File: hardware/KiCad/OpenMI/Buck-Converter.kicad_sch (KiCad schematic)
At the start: 15 parts, among them U6 LM5163

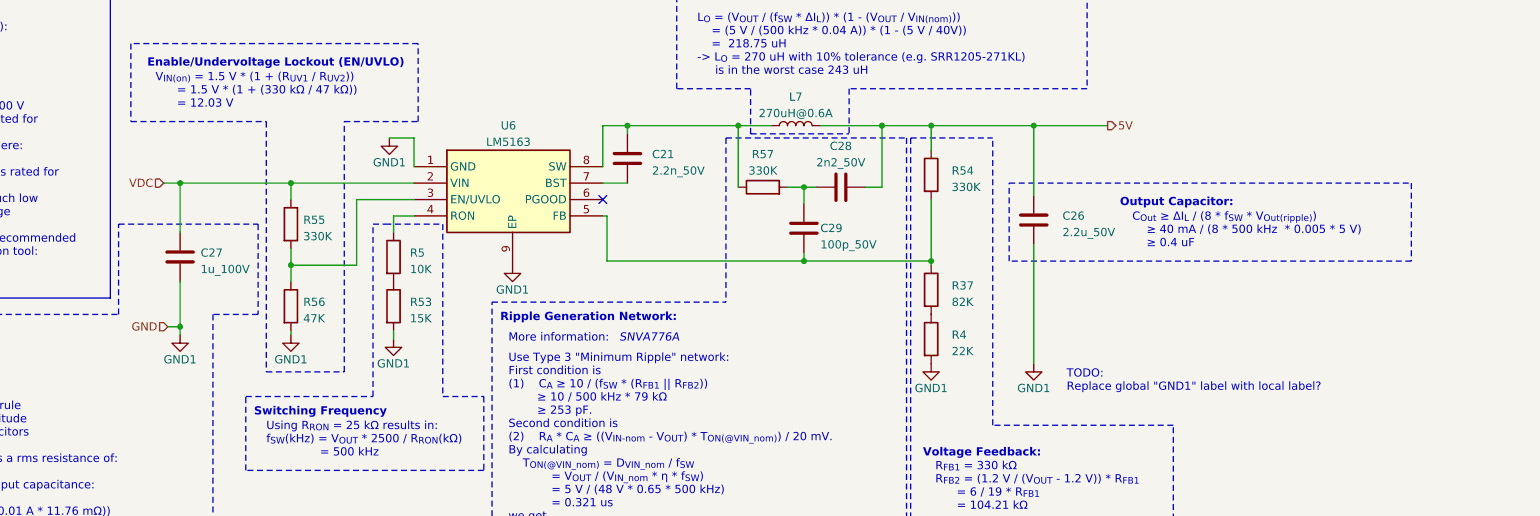
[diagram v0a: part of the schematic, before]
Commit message: refactor(hw): uses new symbol for `LM5163` buck converter
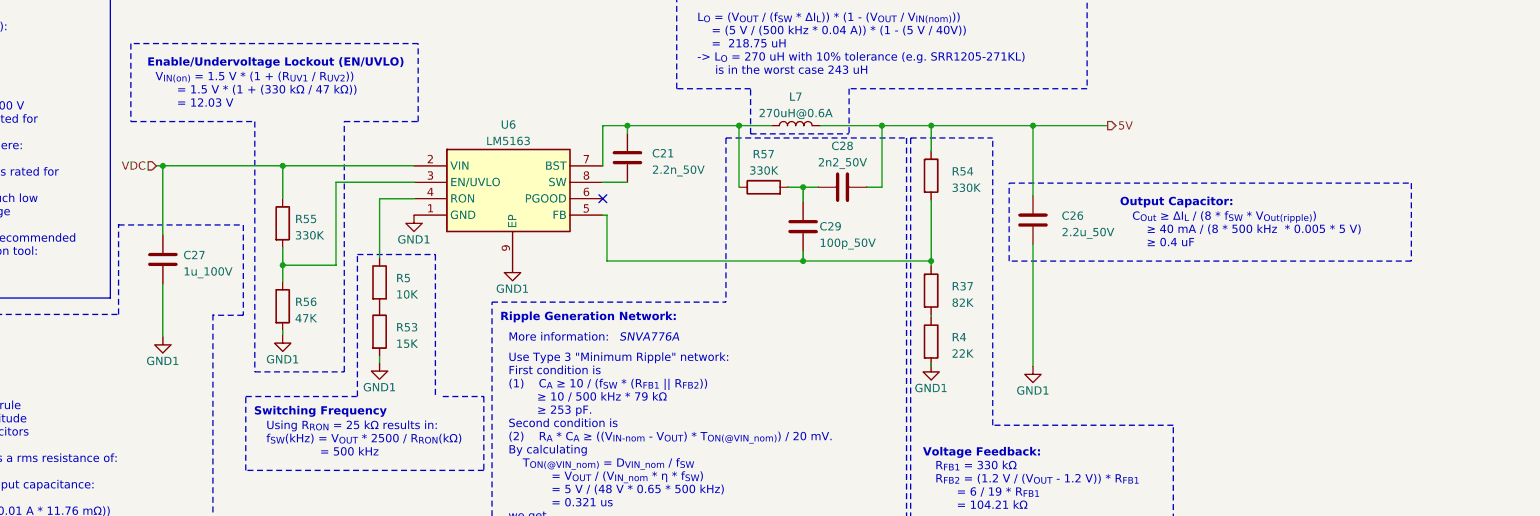
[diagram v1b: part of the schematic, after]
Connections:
- net at C21.1, L7.1, R57.1: now also U6.7 (BST); no longer U6.8 (SW)
- net at C21.2: now also U6.8 (SW); no longer U6.7 (BST)
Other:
- note removed: "TODO: Replace global "GND1" label with local label?"
- moved on the sheet: C27, R5, R53, R55, R56

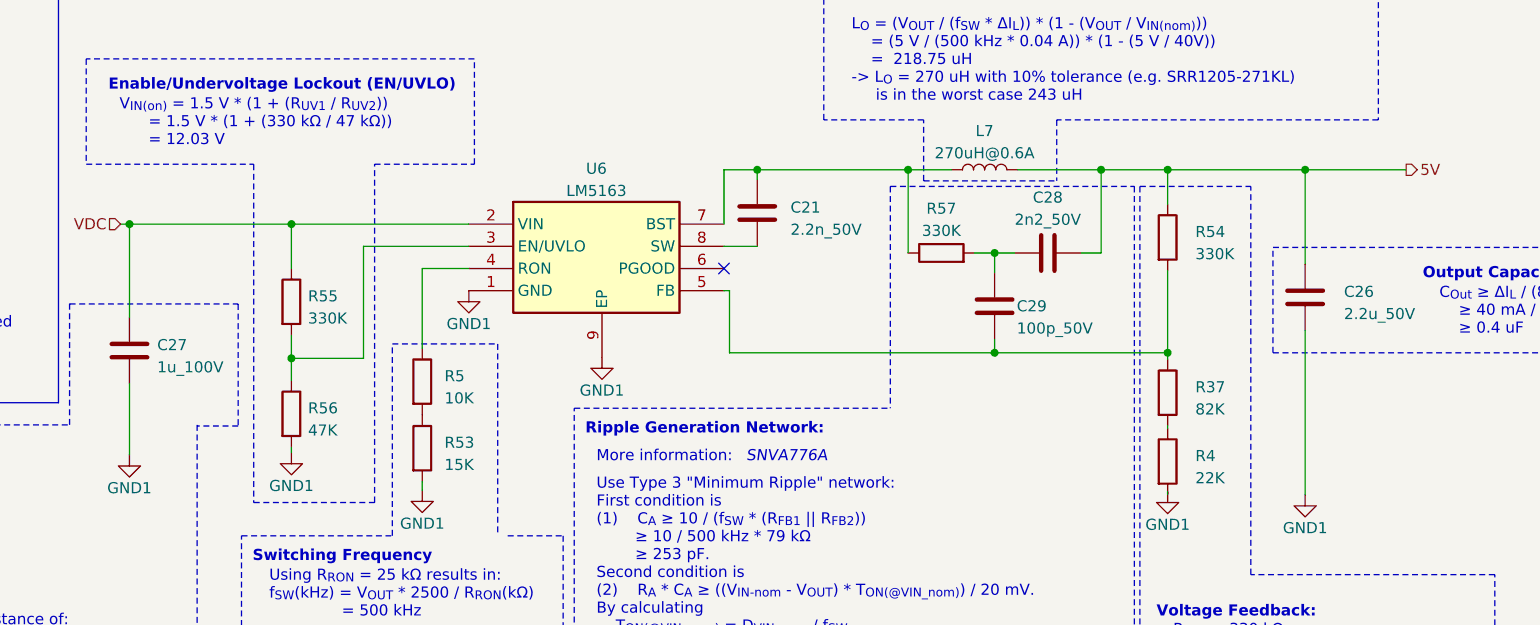
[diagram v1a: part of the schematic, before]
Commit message: chore(hw): updates project to KiCad 8
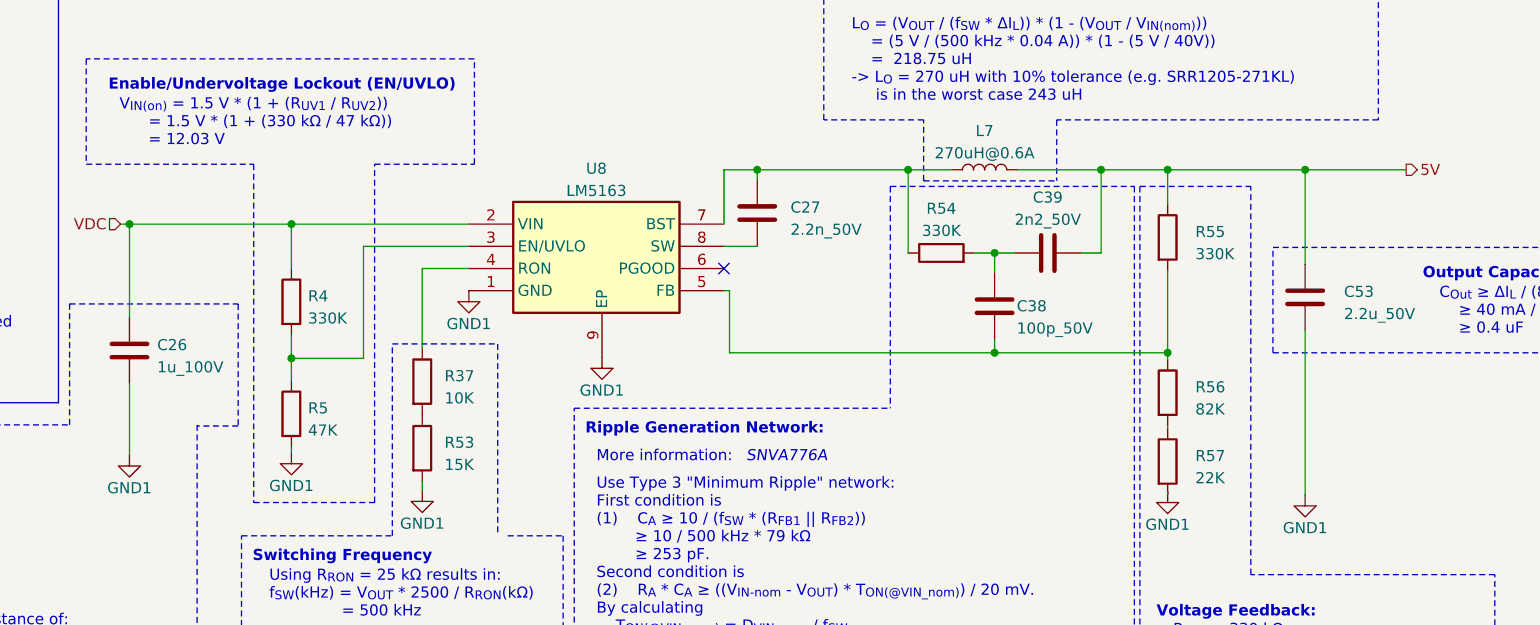
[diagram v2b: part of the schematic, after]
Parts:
- renumbered C27 to C26, C21 to C27, C29 to C38, C28 to C39, C26 to C53, R5 to R37, R55 to R4, R56 to R5, R57 to R54, R54 to R55, R37 to R56, R4 to R57, U6 to U8
